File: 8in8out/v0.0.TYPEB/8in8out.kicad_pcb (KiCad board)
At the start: 2 copper layers, 100.1 x 86.4 mm, 61 parts, among them IC1 ATTINY48-A, J1 RJ45, J2 RJ45, J3 CONN_6, K110 G5T-1-12VDC, K120 G5T-1-12VDC, K130 G5T-1-12VDC, K140 G5T-1-12VDC, K150 G5T-1-12VDC, K160 G5T-1-12VDC, K170 G5T-1-12VDC, K180 G5T-1-12VDC, P1 CONN_5, P100 CONN_2, P101 CONN_2, P102 CONN_2, P103 CONN_2, P105 CONN_2, P106 CONN_2, P110 CONN_2, P120 CONN_2, P130 CONN_2, P140 CONN_2, P150 CONN_2, P160 CONN_2, P170 CONN_2, P180 CONN_2, P2 CONN_5, P3 CONN_10X2, P4 CONN_2, U1 7805, U10 OPTO-TRANSISTOR, U2 ULN2803, U20 OPTO-TRANSISTOR, U30 OPTO-TRANSISTOR, U40 OPTO-TRANSISTOR, U50 OPTO-TRANSISTOR, U60 OPTO-TRANSISTOR, U70 OPTO-TRANSISTOR, U80 OPTO-TRANSISTOR

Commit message: correction RJ45
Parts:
- J1, J2: footprint RJ45_8 -> RJ45_BASIC
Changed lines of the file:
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@@
-    )
-  )
-  (module RJ45_8 (layer Dessus)
-    (at 255.016 149.606)
-    (tags RJ45)
-    (fp_text reference J2 (at 0.254 4.826) (layer F.SilkS)
-      (effects (font (size 1.27 1.27) (thickness 0.3048)))
-    )
-    (fp_text value RJ45 (at 0.14224 -0.1016) (layer F.SilkS)
-      (effects (font (size 1.00076 1.00076) (thickness 0.2032)))
-    )
-    (fp_line (start -7.62 7.874) (end 7.62 7.874) (layer F.SilkS) (width 0.127))
-    (fp_line (start 7.62 7.874) (end 7.62 -10.16) (layer F.SilkS) (width 0.127))
-    (fp_line (start 7.62 -10.16) (end -7.62 -10.16) (layer F.SilkS) (width 0.127))
-    (fp_line (start -7.62 -10.16) (end -7.62 7.874) (layer F.SilkS) (width 0.127))
-    (pad Hole np_thru_hole circle (at 5.93852 0) (size 3.64998 3.64998) (drill 3.251199)
-      (layers *.Cu *.SilkS *.Mask)
-    )
-    (pad Hole np_thru_hole circle (at -5.9309 0) (size 3.64998 3.64998) (drill 3.251199)
-      (layers *.Cu *.SilkS *.Mask)
-    )
-    (pad 1 thru_hole rect (at -4.445 -6.35) (size 1.50114 1.50114) (drill 0.899159)
-      (layers *.Cu *.Mask F.SilkS)
-      (net 94 SDA)
-    )
-    (pad 2 thru_hole circle (at -3.175 -8.89) (size 1.50114 1.50114) (drill 0.899159)
-      (layers *.Cu *.Mask F.SilkS)
-      (net 35 GND)
-    )
-    (pad 3 thru_hole circle (at -1.905 -6.35) (size 1.50114 1.50114) (drill 0.899159)
-      (layers *.Cu *.Mask F.SilkS)
-      (net 93 SCL)
-    )
-    (pad 4 thru_hole circle (at -0.635 -8.89) (size 1.50114 1.50114) (drill 0.899159)
-      (layers *.Cu *.Mask F.SilkS)
-      (net 35 GND)
-    )
-    (pad 5 thru_hole circle (at 0.635 -6.35) (size 1.50114 1.50114) (drill 0.899159)
-      (layers *.Cu *.Mask F.SilkS)
-      (net 19 /INT)
-    )
-    (pad 6 thru_hole circle (at 1.905 -8.89) (size 1.50114 1.50114) (drill 0.899159)
-      (layers *.Cu *.Mask F.SilkS)
-      (net 35 GND)
-    )
-    (pad 7 thru_hole circle (at 3.175 -6.35) (size 1.50114 1.50114) (drill 0.899159)
-      (layers *.Cu *.Mask F.SilkS)
-      (net 20 5V_EXT)
-    )
-    (pad 8 thru_hole circle (at 4.445 -8.89) (size 1.50114 1.50114) (drill 0.899159)
-      (layers *.Cu *.Mask F.SilkS)
-      (net 20 5V_EXT)
-    )
-    (model connectors/RJ45_8.wrl
-      (at (xyz 0 0 0))
-      (scale (xyz 0.4 0.4 0.4))
-      (rotate (xyz 0 0 0))
-    )
-  )
-  (module RJ45_8 (layer Dessus)
-    (at 271.78 149.606)
-    (tags RJ45)
-    (fp_text reference J1 (at 0.254 4.826) (layer F.SilkS)
-      (effects (font (size 1.27 1.27) (thickness 0.3175)))
-    )
-    (fp_text value RJ45 (at 0.14224 -0.1016) (layer F.SilkS)
-      (effects (font (size 1.00076 1.00076) (thickness 0.2032)))
-    )
-    (fp_line (start -7.62 7.874) (end 7.62 7.874) (layer F.SilkS) (width 0.127))
-    (fp_line (start 7.62 7.874) (end 7.62 -10.16) (layer F.SilkS) (width 0.127))
-    (fp_line (start 7.62 -10.16) (end -7.62 -10.16) (layer F.SilkS) (width 0.127))
-    (fp_line (start -7.62 -10.16) (end -7.62 7.874) (layer F.SilkS) (width 0.127))
-    (pad Hole np_thru_hole circle (at 5.93852 0) (size 3.64998 3.64998) (drill 3.251199)
-      (layers *.Cu *.SilkS *.Mask)
-    )
-    (pad Hole np_thru_hole circle (at -5.9309 0) (size 3.64998 3.64998) (drill 3.251199)
-      (layers *.Cu *.SilkS *.Mask)
-    )
-    (pad 1 thru_hole rect (at -4.445 -6.35) (size 1.50114 1.50114) (drill 0.899159)
-      (layers *.Cu *.Mask F.SilkS)
-      (net 94 SDA)
-    )
-    (pad 2 thru_hole circle (at -3.175 -8.89) (size 1.50114 1.50114) (drill 0.899159)
-      (layers *.Cu *.Mask F.SilkS)
-      (net 35 GND)
-    )
-    (pad 3 thru_hole circle (at -1.905 -6.35) (size 1.50114 1.50114) (drill 0.899159)
-      (layers *.Cu *.Mask F.SilkS)
-      (net 93 SCL)
-    )
-    (pad 4 thru_hole circle (at -0.635 -8.89) (size 1.50114 1.50114) (drill 0.899159)
-      (layers *.Cu *.Mask F.SilkS)
-      (net 35 GND)
-    )
-    (pad 5 thru_hole circle (at 0.635 -6.35) (size 1.50114 1.50114) (drill 0.899159)
-      (layers *.Cu *.Mask F.SilkS)
-      (net 19 /INT)
-    )
-    (pad 6 thru_hole circle (at 1.905 -8.89) (size 1.50114 1.50114) (drill 0.899159)
-      (layers *.Cu *.Mask F.SilkS)
-      (net 35 GND)
-    )
-    (pad 7 thru_hole circle (at 3.175 -6.35) (size 1.50114 1.50114) (drill 0.899159)
-      (layers *.Cu *.Mask F.SilkS)
-      (net 20 5V_EXT)
-    )
-    (pad 8 thru_hole circle (at 4.445 -8.89) (size 1.50114 1.50114) (drill 0.899159)
-      (layers *.Cu *.Mask F.SilkS)
-      (net 20 5V_EXT)
-    )
-    (model connectors/RJ45_8.wrl
-      (at (xyz 0 0 0))
-      (scale (xyz 0.4 0.4 0.4))
-      (rotate (xyz 0 0 0))
     )
   )
@@
       (rotate (xyz 0 0 0))
     )
+  )
+  (module RJ45_BASIC (layer Dessus)
+    (at 271.78 149.606)
+    (tags RJ45)
+    (fp_text reference J1 (at 0.254 4.826) (layer F.SilkS)
+      (effects (font (thickness 0.3048)))
+    )
+    (fp_text value RJ45 (at 0.14224 -0.1016) (layer F.SilkS)
+      (effects (font (size 1.00076 1.00076) (thickness 0.2032)))
+    )
+    (fp_line (start -7.62 7.874) (end 7.62 7.874) (layer F.SilkS) (width 0.127))
+    (fp_line (start 7.62 7.874) (end 7.62 -10.16) (layer F.SilkS) (width 0.127))
+    (fp_line (start 7.62 -10.16) (end -7.62 -10.16) (layer F.SilkS) (width 0.127))
+    (fp_line (start -7.62 -10.16) (end -7.62 7.874) (layer F.SilkS) (width 0.127))
+    (pad Hole thru_hole circle (at 5.93852 0) (size 3.64998 3.64998) (drill 3.2512)
+      (layers *.Cu *.Mask F.SilkS)
+    )
+    (pad Hole thru_hole circle (at -5.9309 0) (size 3.64998 3.64998) (drill 3.2512)
+      (layers *.Cu *.Mask F.SilkS)
+    )
+    (pad 1 thru_hole rect (at -4.445 -6.35) (size 1.50114 1.50114) (drill 0.89916)
+      (layers *.Cu *.Mask F.SilkS)
+      (net 94 SDA)
+    )
+    (pad 2 thru_hole circle (at -3.175 -8.89) (size 1.50114 1.50114) (drill 0.89916)
+      (layers *.Cu *.Mask F.SilkS)
+      (net 35 GND)
+    )
+    (pad 3 thru_hole circle (at -1.905 -6.35) (size 1.50114 1.50114) (drill 0.89916)
+      (layers *.Cu *.Mask F.SilkS)
+      (net 93 SCL)
+    )
+    (pad 4 thru_hole circle (at -0.635 -8.89) (size 1.50114 1.50114) (drill 0.89916)
+      (layers *.Cu *.Mask F.SilkS)
+      (net 35 GND)
+    )
+    (pad 5 thru_hole circle (at 0.635 -6.35) (size 1.50114 1.50114) (drill 0.89916)
+      (layers *.Cu *.Mask F.SilkS)
+      (net 19 /INT)
+    )
+    (pad 6 thru_hole circle (at 1.905 -8.89) (size 1.50114 1.50114) (drill 0.89916)
+      (layers *.Cu *.Mask F.SilkS)
+      (net 35 GND)
+    )
+    (pad 7 thru_hole circle (at 3.175 -6.35) (size 1.50114 1.50114) (drill 0.89916)
+      (layers *.Cu *.Mask F.SilkS)
+      (net 20 5V_EXT)
+    )
+    (pad 8 thru_hole circle (at 4.445 -8.89) (size 1.50114 1.50114) (drill 0.89916)
+      (layers *.Cu *.Mask F.SilkS)
+      (net 20 5V_EXT)
+    )
+    (model connectors/RJ45_8.wrl
+      (at (xyz 0 0 0))
+      (scale (xyz 0.4 0.4 0.4))
+      (rotate (xyz 0 0 0))
+    )
+  )
+  (module RJ45_BASIC (layer Dessus)
+    (at 255.016 149.606)
+    (tags RJ45)
+    (fp_text reference J2 (at 0.254 4.826) (layer F.SilkS)
+      (effects (font (thickness 0.3048)))
+    )
+    (fp_text value RJ45 (at 0.14224 -0.1016) (layer F.SilkS)
+      (effects (font (size 1.00076 1.00076) (thickness 0.2032)))
+    )
+    (fp_line (start -7.62 7.874) (end 7.62 7.874) (layer F.SilkS) (width 0.127))
+    (fp_line (start 7.62 7.874) (end 7.62 -10.16) (layer F.SilkS) (width 0.127))
+    (fp_line (start 7.62 -10.16) (end -7.62 -10.16) (layer F.SilkS) (width 0.127))
+    (fp_line (start -7.62 -10.16) (end -7.62 7.874) (layer F.SilkS) (width 0.127))
+    (pad Hole thru_hole circle (at 5.93852 0) (size 3.64998 3.64998) (drill 3.2512)
+      (layers *.Cu *.Mask F.SilkS)
+    )
+    (pad Hole thru_hole circle (at -5.9309 0) (size 3.64998 3.64998) (drill 3.2512)
+      (layers *.Cu *.Mask F.SilkS)
+    )
+    (pad 1 thru_hole rect (at -4.445 -6.35) (size 1.50114 1.50114) (drill 0.89916)
+      (layers *.Cu *.Mask F.SilkS)
+      (net 94 SDA)
+    )
+    (pad 2 thru_hole circle (at -3.175 -8.89) (size 1.50114 1.50114) (drill 0.89916)
+      (layers *.Cu *.Mask F.SilkS)
+      (net 35 GND)
+    )
+    (pad 3 thru_hole circle (at -1.905 -6.35) (size 1.50114 1.50114) (drill 0.89916)
+      (layers *.Cu *.Mask F.SilkS)
+      (net 93 SCL)
+    )
+    (pad 4 thru_hole circle (at -0.635 -8.89) (size 1.50114 1.50114) (drill 0.89916)
+      (layers *.Cu *.Mask F.SilkS)
+      (net 35 GND)
+    )
+    (pad 5 thru_hole circle (at 0.635 -6.35) (size 1.50114 1.50114) (drill 0.89916)
+      (layers *.Cu *.Mask F.SilkS)
+      (net 19 /INT)
+    )
+    (pad 6 thru_hole circle (at 1.905 -8.89) (size 1.50114 1.50114) (drill 0.89916)
+      (layers *.Cu *.Mask F.SilkS)
+      (net 35 GND)
+    )
+    (pad 7 thru_hole circle (at 3.175 -6.35) (size 1.50114 1.50114) (drill 0.89916)
+      (layers *.Cu *.Mask F.SilkS)
+      (net 20 5V_EXT)
+    )
+    (pad 8 thru_hole circle (at 4.445 -8.89) (size 1.50114 1.50114) (drill 0.89916)
+      (layers *.Cu *.Mask F.SilkS)
+      (net 20 5V_EXT)
+    )
+    (model connectors/RJ45_8.wrl
+      (at (xyz 0 0 0))
+      (scale (xyz 0.4 0.4 0.4))
+      (rotate (xyz 0 0 0))
+    )

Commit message: modif mineure
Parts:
- moved P1 1.64 mm to (186.7, 151.5)
- moved P2 1.64 mm to (208.3, 151.5)
- moved P105 0.90 mm to (241.7, 150.6)
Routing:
- net IN0: track 33.4 -> 38.5 mm
- net +12V: track 221.5 -> 224.8 mm
- net COM0: track 75.7 -> 78.7 mm
- net IN1: track 11.4 -> 14.3 mm
- net IN2: track 10.2 -> 12.8 mm
- net IN6: track 17.7 -> 20.1 mm
- net IN3: track 12.1 -> 13.8 mm
- net IN5: track 15.6 -> 17.2 mm
- net IN7: track 20.7 -> 22.4 mm
- net COM1: track 37.9 -> 38.6 mm
- net GND: track 50.0 -> 50.5 mm
- added copper zone on F.Cu, net /230_120_1
- added copper zone on F.Cu, net /230_120_2
- added copper zone on F.Cu, net /230_130_1
- added copper zone on F.Cu, net /230_130_2
- added copper zone on F.Cu, net /230_140_1
- added copper zone on F.Cu, net /230_140_2
- added copper zone on F.Cu, net /230_150_1
- added copper zone on F.Cu, net /230_150_2
- added copper zone on F.Cu, net /230_160_1
- added copper zone on F.Cu, net /230_160_2
- added copper zone on F.Cu, net /230_170_1
- added copper zone on F.Cu, net /230_170_2
- added copper zone on F.Cu, net /230_180_1
- added copper zone on F.Cu, net /230_180_2
- removed copper zone on B.Cu, net /230_110_1
- removed copper zone on B.Cu, net /230_110_2

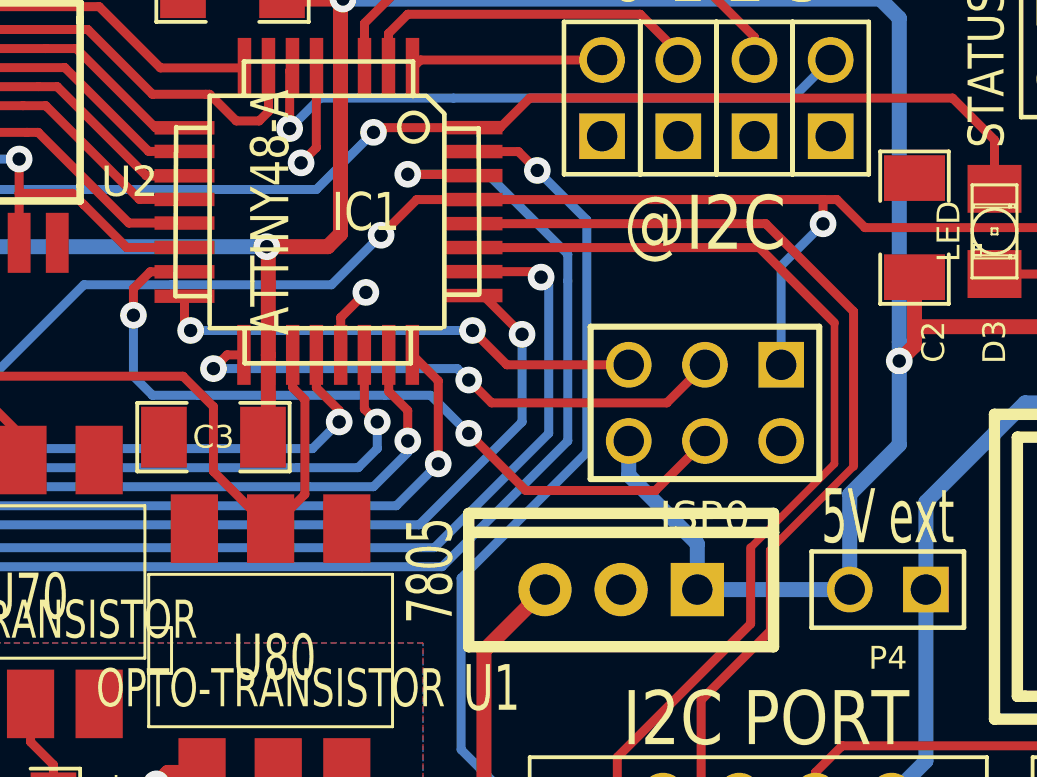
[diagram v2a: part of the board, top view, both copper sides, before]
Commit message: correction connecteur ISP
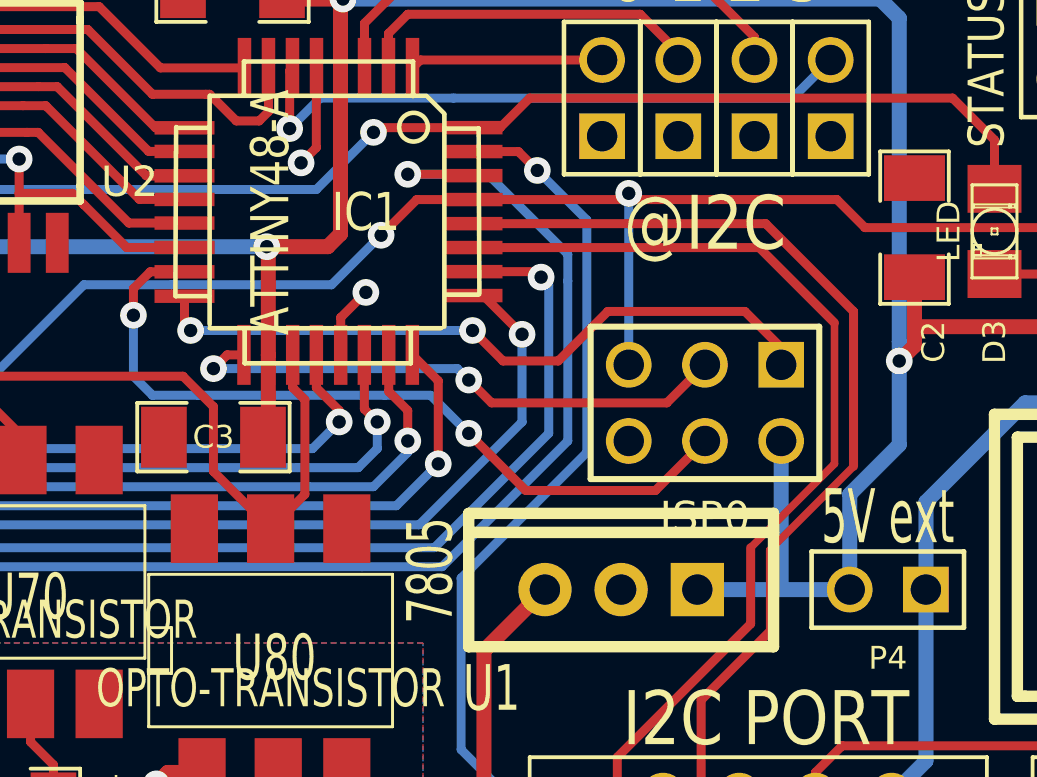
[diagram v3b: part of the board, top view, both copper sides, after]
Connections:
- ISP0 pad 1: RESET -> MISO
- ISP0 pad 2: GND -> +5V
- ISP0 pad 5: MISO -> RESET
- ISP0 pad 6: +5V -> GND
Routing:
- net MISO: track 16.3 -> 23.1 mm
- net +5V: track 116.1 -> 115.2 mm
